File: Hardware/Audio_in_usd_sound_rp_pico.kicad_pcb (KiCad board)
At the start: 2 copper layers, 100 x 100 mm, 275 parts, among them J1 ADC IN, J11 SDR ANT, J12 SDR Out, J13 ANT_BNC, J14 ANT_BNC, J15 Audio IN, J16 Audio IN, J17 Mini-jack socket, J4 Conn_02x20_Counter_Clockwise, J5 Conn_01x20, J6 Conn_01x20, J7 Conn_02x20_Counter_Clockwise, J8 BNC, Q1 MMBT2222A 1P, Q2 MMBT2222A 1P, Q3 MMBT2222A, SW1 Left, SW2 Right, T1 Screw Terminal, 4Px5.08mm, 20A, T2 Screw Terminal, 4Px5.08mm, 20A, U1 LSM6DSO32TR, U10 Si4732, U11 HS96L03W2C03, U12 L298N, U13 LM393DR2G, U15 DS18B20A10T6, U17 LM2937xS, U2 PCM1808PWR, U3 Pico, U4 MS5351M, U5 CJ431, U6 TSOP4438, U7 PI5C3253CQEX, U8 OPA1612AxD, U9 LM358, X1 Q13FC1350000400, Y1 X322525MSB4SI

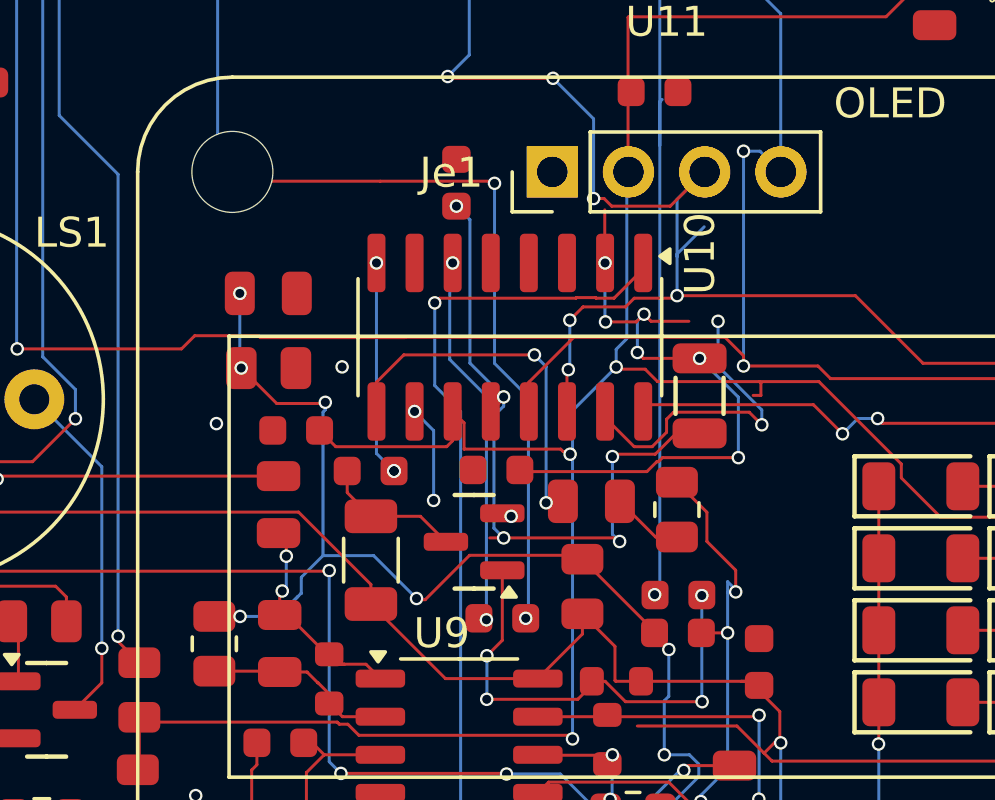
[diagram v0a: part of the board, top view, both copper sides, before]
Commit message: Si4732 Schematic and PCB revision
Modified schematic and PCB of Si4732 chip to correct the order of pins 9-16.
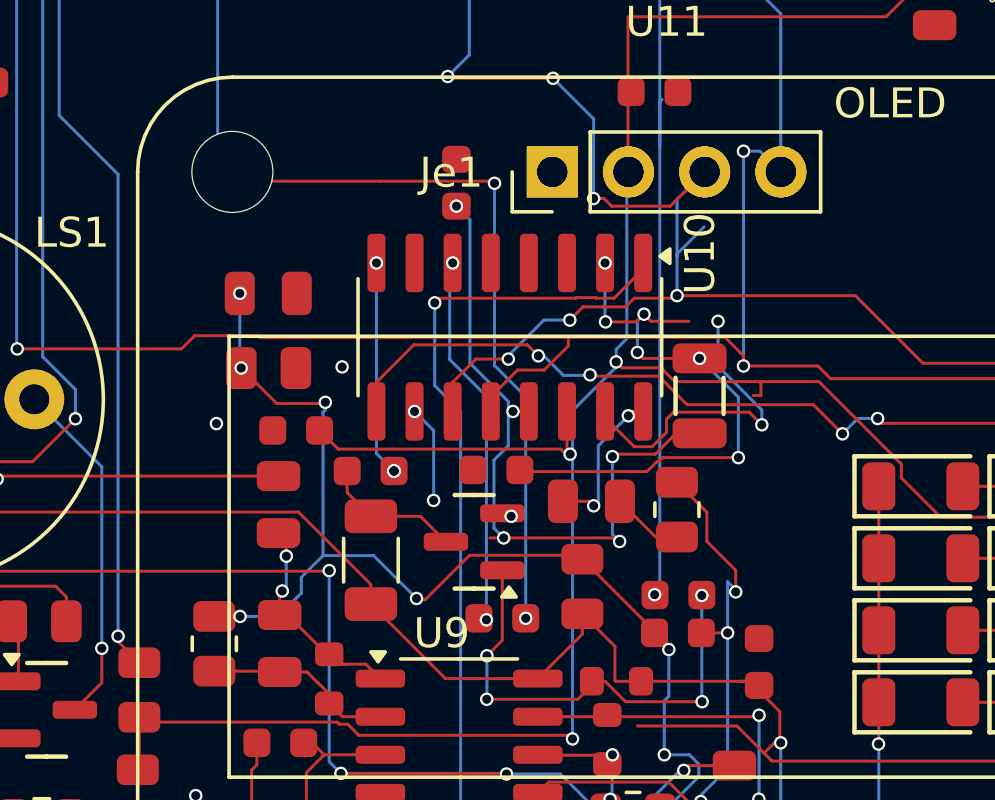
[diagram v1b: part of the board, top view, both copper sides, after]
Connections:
- net <NO NET> renamed ~
- C45 pad 2: Net-(U10-ROUT) -> Net-(C45-Pad2)
- U10 pad 11: +3.3V -> /SCL
- U10 pad 12: Net-(U10-RCLK) -> /SDA
- U10 pad 13: /SDA -> Net-(U10-RCLK)
- U10 pad 14: /SCL -> +3.3V
- U10 pad 16: /~{RST} -> Net-(C45-Pad2)
- U10 pad 9: Net-(U10-ROUT) -> /~{RST}
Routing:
- net Net-(U10-ROUT): track 12.3 -> 0.00 mm, vias 2 -> 0
- net /~{RST}: track 57.6 -> 68.8 mm, vias 3 -> 5
- net Net-(C45-Pad2): track 0.00 -> 5.53 mm, vias 0 -> 2
- net /SCL: track 214.3 -> 217.0 mm
- net Net-(U10-DCLK): track 21.4 -> 19.7 mm
- net /SDA: track 292.2 -> 293.2 mm
- net +3.3V: track 415.0 -> 414.5 mm
